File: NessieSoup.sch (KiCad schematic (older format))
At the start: 4 parts, among them CN1 PLUS4_USERPORT, CN2 CONN_SNES_1, CN3 CONN_SNES_2, J1 CONN_NES

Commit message: Almost there
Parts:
- added V0: LICENSE, NessieSoup:cc_by_nc_sa_small, symbol void:Void
- added V1: LOGO1, NessieSoup:Logo1, symbol void:Void
- added V2: LOGO2, NessieSoup:Logo2, symbol void:Void
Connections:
- net labels added: port1_d0, port2_d0, port2_d1, port2_pp
- net labels removed: data1, data2
- wire segments 45 -> 43
- no-connect marks 15 -> 20
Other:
- note added: "These 2 signals make\nMultiTap support possible"
- note added: "This port is compatible\nwith the Attack of the\nPETSCII Robots adapter"
- note removed: "MULTITAP"
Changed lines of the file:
@@
 encoding utf-8
 Sheet 1 1
-Title ""
-Date ""
-Rev ""
-Comp ""
-Comment1 ""
-Comment2 ""
+Title "NessieSoup"
+Date "2024-07-08"
+Rev "1git"
+Comp "SukkoPera"
+Comment1 "Licensed under CC BY-NC-SA 4.0"
+Comment2 "https://github.com/SukkoPera/NessieSoup"
 Comment3 ""
 Comment4 ""
@@
 	2075 2285 1670 2285
 Wire Wire Line
-	2075 2385 1670 2385
-Wire Wire Line
-	2075 2485 1670 2485
-Wire Wire Line
 	3575 1985 3980 1985
 Wire Wire Line
@@
 latch
 Text Label 8500 2195 2    50   ~ 0
-data1
-Text Notes 8580 2325 0    50   ~ 0
-MULTITAP
+port1_d0
+Text Notes 10080 2390 0    50   ~ 0
+These 2 signals make\nMultiTap support possible
 Text Notes 7965 1995 0    50   ~ 0
 cup
@@
 NoConn ~ 7340 2395
 Text Label 3980 2685 2    50   ~ 0
-data1
+port1_d0
 Text Label 3980 2385 2    50   ~ 0
 clock
@@
 latch
 Text Label 3980 1985 2    50   ~ 0
-data2
+port2_d0
 Wire Wire Line
 	9360 1995 10005 1995
@@
 latch
 Text Label 10005 2195 2    50   ~ 0
-data2
+port2_d0
 Text Notes 9470 1995 0    50   ~ 0
 cup
@@
 	1    0    0    -1
 $EndComp
+Text Label 10005 2295 2    50   ~ 0
+port2_d1
+NoConn ~ 2075 2085
+NoConn ~ 8500 2295
+NoConn ~ 8500 2395
+Text Label 10005 2395 2    50   ~ 0
+port2_pp
+Wire Notes Line
+	9665 2215 10040 2215
+Wire Notes Line
+	10040 2215 10040 2440
+Wire Notes Line
+	10040 2440 9665 2440
+Wire Notes Line
+	9665 2440 9665 2215
+Text Notes 7655 1560 0    50   ~ 0
+This port is compatible\nwith the Attack of the\nPETSCII Robots adapter
+Text Label 1670 2185 0    50   ~ 0
+port2_d1
+Text Label 1670 2285 0    50   ~ 0
+port2_pp
+NoConn ~ 2075 2385
+NoConn ~ 2075 2485
+$Comp
+L void:Void V0
+U 1 1 668D5315
+P 10705 5985
+F 0 "V0" H 10783 6031 50  0000 L CNN
+F 1 "LICENSE" H 10783 5940 50  0000 L CNN
+F 2 "NessieSoup:cc_by_nc_sa_small" H 10705 5985 50  0001 C CNN
+F 3 "" H 10705 5985 50  0001 C CNN
+	1    10705 5985
+	1    0    0    -1
+$EndComp
+$Comp
+L void:Void V1
+U 1 1 668D668E
+P 10705 6170
+F 0 "V1" H 10783 6216 50  0000 L CNN
+F 1 "LOGO1" H 10783 6125 50  0000 L CNN
+F 2 "NessieSoup:Logo1" H 10705 6170 50  0001 C CNN
+F 3 "" H 10705 6170 50  0001 C CNN
+	1    10705 6170
+	1    0    0    -1
+$EndComp
+$Comp
+L void:Void V2
+U 1 1 668D6AB2
+P 10705 6350
+F 0 "V2" H 10783 6396 50  0000 L CNN
+F 1 "LOGO2" H 10783 6305 50  0000 L CNN
+F 2 "NessieSoup:Logo2" H 10705 6350 50  0001 C CNN
+F 3 "" H 10705 6350 50  0001 C CNN
+	1    10705 6350
+	1    0    0    -1
+$EndComp

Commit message: Add capacitor Yeah, we must have at least one component...
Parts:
- added C1: 47u, Capacitor_THT:CP_Radial_D5.0mm_P2.00mm, symbol Device:CP1
- renumbered J1 to CN99
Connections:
- net +5V: now also C1.1
- net GND: now also C1.2
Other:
- note added: "Currently unused, but\nif we ever want to make\na NES version, this is\nthe pinout to be used"
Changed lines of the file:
@@
 P 6495 2195
 AR Path="/668C296F/668DE1D4" Ref="J?"  Part="1"
-AR Path="/668DE1D4" Ref="J1"  Part="1"
-F 0 "J1" H 6390 1670 50  0000 C CNN
+AR Path="/668DE1D4" Ref="CN99"  Part="1"
+F 0 "CN99" H 6390 1670 50  0000 C CNN
 F 1 "CONN_NES" H 6445 1760 50  0000 C CNN
 F 2 "" H 6495 2195 50  0001 C CNN
@@
 	1    0    0    -1
 $EndComp
+$Comp
+L Device:CP1 C1
+U 1 1 668DE5DF
+P 7350 3625
+F 0 "C1" H 7465 3671 50  0000 L CNN
+F 1 "47u" H 7465 3580 50  0000 L CNN
+F 2 "Capacitor_THT:CP_Radial_D5.0mm_P2.00mm" H 7350 3625 50  0001 C CNN
+F 3 "~" H 7350 3625 50  0001 C CNN
+	1    7350 3625
+	1    0    0    -1
+$EndComp
+$Comp
+L power:GND #PWR?
+U 1 1 668DF315
+P 7350 3910
+AR Path="/668C296F/668DF315" Ref="#PWR?"  Part="1"
+AR Path="/668DF315" Ref="#PWR0110"  Part="1"
+F 0 "#PWR0110" H 7350 3660 50  0001 C CNN
+F 1 "GND" H 7355 3737 50  0000 C CNN
+F 2 "" H 7350 3910 50  0001 C CNN
+F 3 "" H 7350 3910 50  0001 C CNN
+	1    7350 3910
+	-1   0    0    -1
+$EndComp
+Wire Wire Line
+	7350 3775 7350 3910
+Text Notes 6470 1555 0    50   ~ 0
+Currently unused, but\nif we ever want to make\na NES version, this is\nthe pinout to be used
+Wire Wire Line
+	7350 3475 7350 3365
+$Comp
+L power:+5V #PWR?
+U 1 1 668E102F
+P 7350 3365
+AR Path="/668C296F/668E102F" Ref="#PWR?"  Part="1"
+AR Path="/668E102F" Ref="#PWR0111"  Part="1"
+F 0 "#PWR0111" H 7350 3215 50  0001 C CNN
+F 1 "+5V" H 7365 3538 50  0000 C CNN
+F 2 "" H 7350 3365 50  0001 C CNN
+F 3 "" H 7350 3365 50  0001 C CNN
+	1    7350 3365
+	1    0    0    -1
+$EndComp

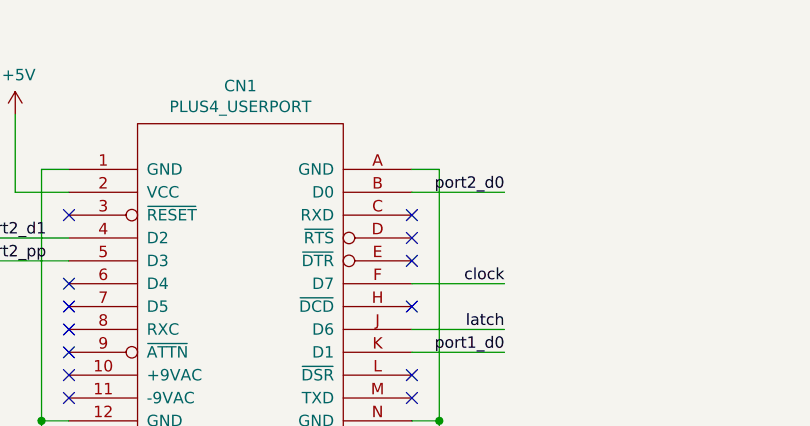
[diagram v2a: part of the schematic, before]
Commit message: Refine shape
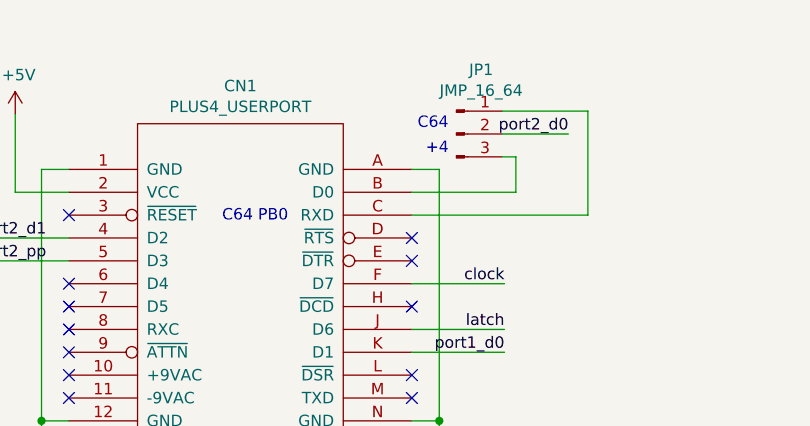
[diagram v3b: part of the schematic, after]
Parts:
- added JP1: JMP_16_64, Connector_PinHeader_2.54mm:PinHeader_1x03_P2.54mm_Vertical, symbol Connector:Conn_01x03_Male
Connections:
- net port2_d0: now also JP1.2 (Pin_2); no longer CN1.B (D0)
- net at CN1.C (RXD): now also JP1.1 (Pin_1)
- new net: CN1.B (D0), JP1.3 (Pin_3)
- no-connect marks 20 -> 19
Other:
- note added: "+4"
- note added: "C64"
- note added: "C64 PB0"
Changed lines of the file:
@@
 NoConn ~ 3575 2785
 NoConn ~ 3575 2885
-NoConn ~ 3575 2085
 NoConn ~ 3575 2185
 NoConn ~ 3575 2285
@@
 Wire Wire Line
 	2075 2285 1670 2285
-Wire Wire Line
-	3575 1985 3980 1985
 Wire Wire Line
 	3575 2385 3980 2385
@@
 Text Label 3980 2585 2    50   ~ 0
 latch
-Text Label 3980 1985 2    50   ~ 0
+Text Label 4260 1730 2    50   ~ 0
 port2_d0
 Wire Wire Line
@@
 	1    0    0    -1
 $EndComp
+$Comp
+L Connector:Conn_01x03_Male JP1
+U 1 1 668DD29D
+P 3770 1730
+F 0 "JP1" H 3878 2011 50  0000 C CNN
+F 1 "JMP_16_64" H 3878 1920 50  0000 C CNN
+F 2 "Connector_PinHeader_2.54mm:PinHeader_1x03_P2.54mm_Vertical" H 3770 1730 50  0001 C CNN
+F 3 "~" H 3770 1730 50  0001 C CNN
+	1    3770 1730
+	1    0    0    -1
+$EndComp
+Wire Wire Line
+	3970 1730 4260 1730
+Wire Wire Line
+	3970 1830 4030 1830
+Wire Wire Line
+	4030 1830 4030 1985
+Wire Wire Line
+	3575 1985 4030 1985
+Text Notes 3635 1825 0    50   ~ 0
++4
+Text Notes 3600 1715 0    50   ~ 0
+C64
+Text Notes 2745 2120 0    50   ~ 0
+C64 PB0
+Wire Wire Line
+	3970 1630 4345 1630
+Wire Wire Line
+	4345 1630 4345 2085
+Wire Wire Line
+	4345 2085 3575 2085
 $EndSCHEMATC
